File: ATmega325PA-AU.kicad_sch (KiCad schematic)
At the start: 19 parts, among them J1 1x3 straight header pins, J10 2Pin_Header_2.54, J2 1x3 straight header pins, J3 1x3 straight header pins, J4 1x3 straight header pins, J5 1x3 straight header pins, J6 1x3 straight header pins, J7 1x3 straight header pins, U2 ATMEGA325PA-AU, Y1 ABMM2-7.3728MHZ-E2-T

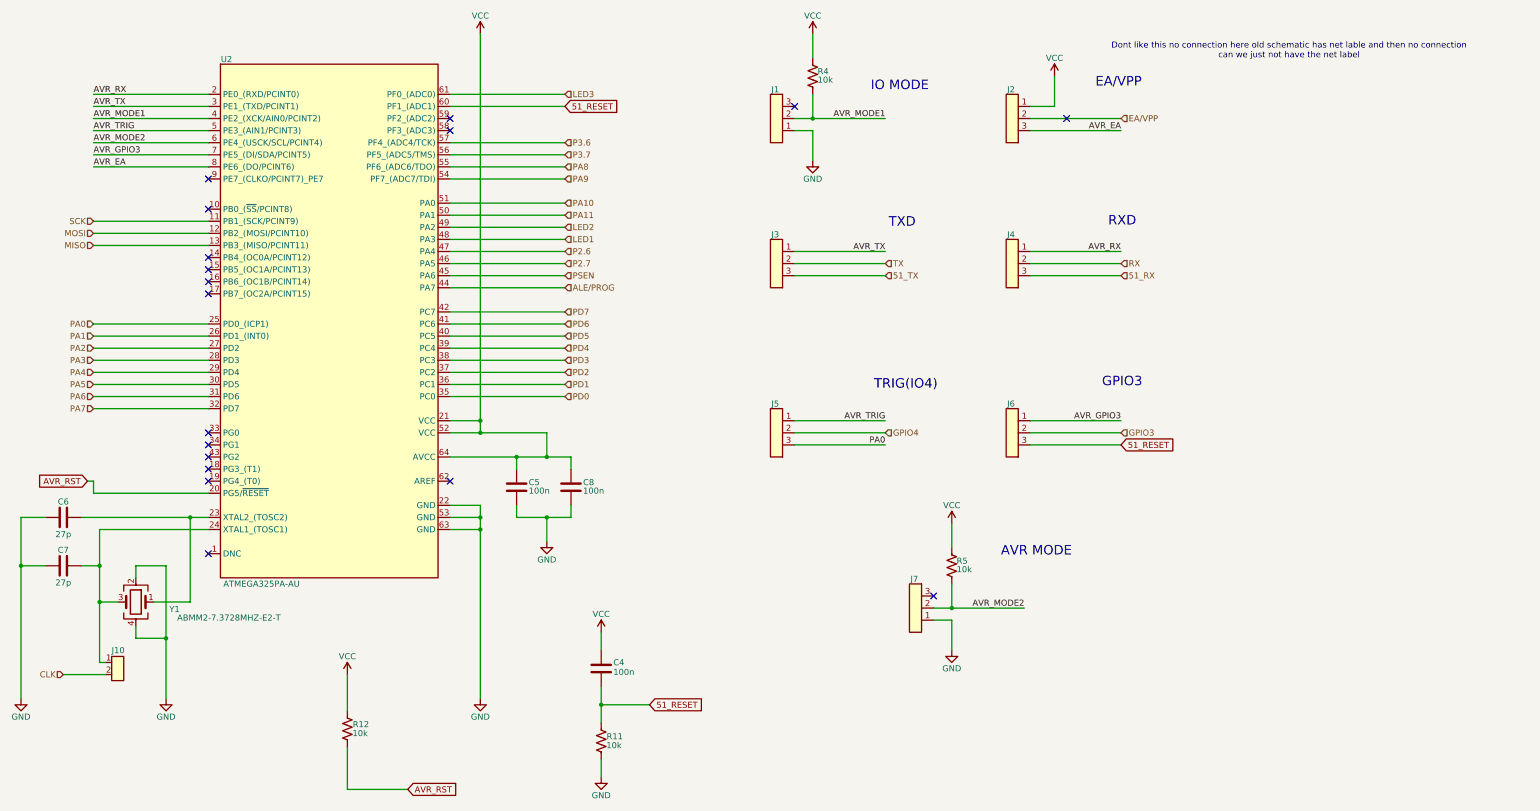
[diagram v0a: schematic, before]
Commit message: updated schematic after library re-organization
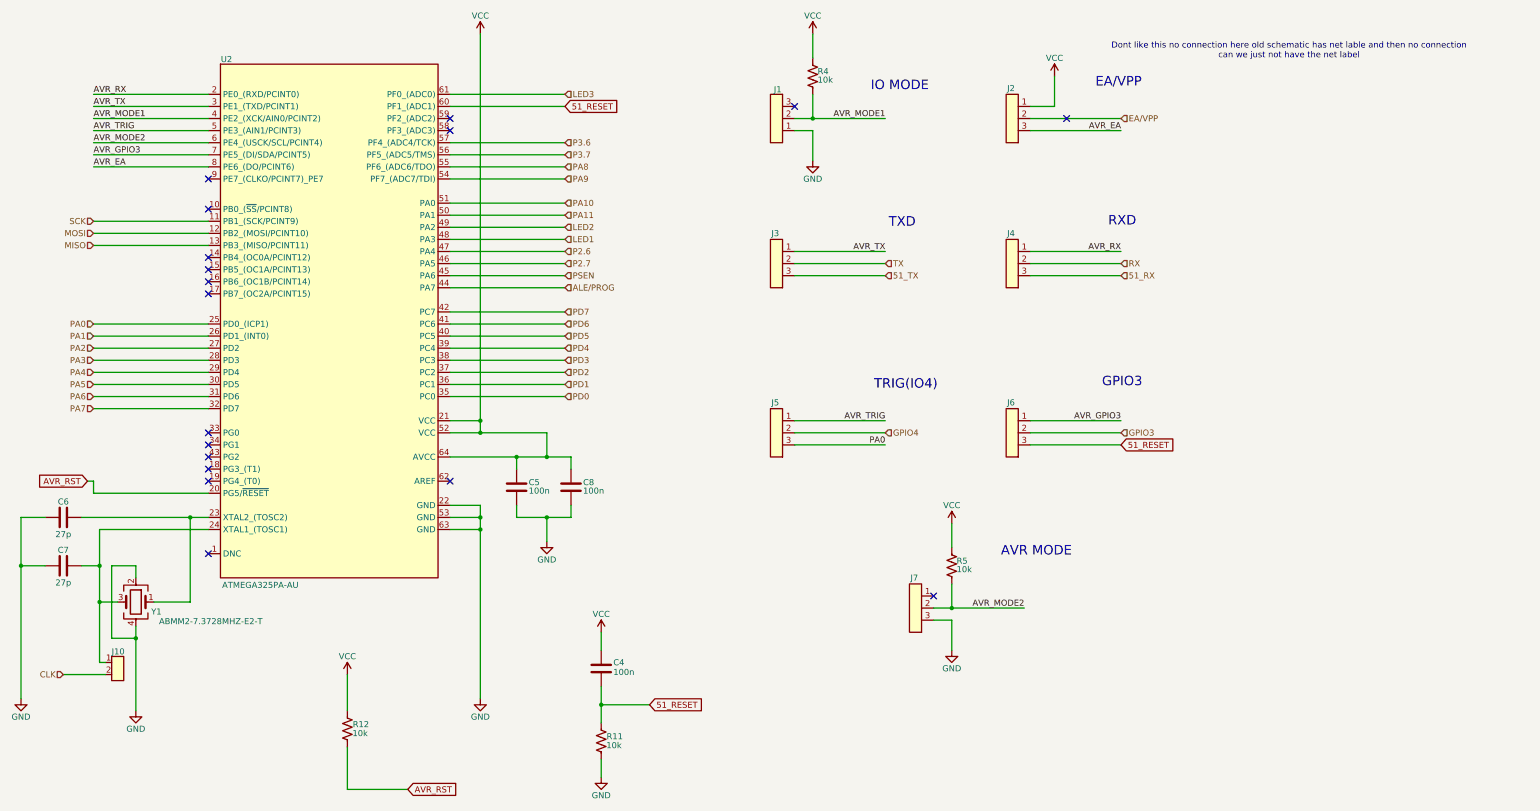
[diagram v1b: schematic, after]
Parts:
- removed J1, J2, J3, J4, J5, J6, J7: 1x3 straight header pins, Connector_PinHeader_2.54mm:PinHeader_1x03_P2.54mm_Vertical, symbol tutorial_2_library:VERT_HDR_3_2.54mm
- removed J10: 2Pin_Header_2.54, Connector_PinHeader_2.54mm:PinHeader_2x01_P2.54mm_Vertical, symbol tutorial_2_library:VERT_HDR_2_2.54mm
- removed U2: ATMEGA325PA-AU, Package_QFP:TQFP-64_10x10mm_P0.5mm, symbol tutorial_2_library:ATMEGA325PA-AU
- removed Y1: ABMM2-7.3728MHZ-E2-T, Crystal:Crystal_SMD_0603-4Pin_6.0x3.5mm, symbol tutorial_2_library:Crystal_7.3728MHZ_SMD
- added J1, J2, J3, J4, J5, J6, J7: 1x3 straight header pins, Connector_PinHeader_2.54mm:PinHeader_1x03_P2.54mm_Vertical, symbol NAE_Connectors:VERT_HDR_3_2.54mm
- added J10: 2Pin_Header_2.54, Connector_PinHeader_2.54mm:PinHeader_2x01_P2.54mm_Vertical, symbol NAE_Connectors:VERT_HDR_2_2.54mm
- added U2: ATMEGA325PA-AU, Package_QFP:TQFP-64_10x10mm_P0.5mm, symbol NAE_Integrated_Circuits:ATMEGA325PA-AU
- added Y1: ABMM2-7.3728MHZ-E2-T, Crystal:Crystal_SMD_0603-4Pin_6.0x3.5mm, symbol NAE_Crystals:Crystal_7.3728MHZ_SMD
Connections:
- net 51_RESET: now also J6.3, U2.60 (PF1_(ADC1))
- net 51_RX: now also J4.3
- net 51_TX: now also J3.3
- net ALE/PROG: now also U2.44 (PA7)
- net AVR_EA: now also J2.3, U2.8 (PE6_(DO/PCINT6))
- net AVR_GPIO3: now also J6.1, U2.7 (PE5_(DI/SDA/PCINT5))
- net AVR_MODE1: now also J1.2, U2.4 (PE2_(XCK/AIN0/PCINT2))
- net AVR_MODE2: now also J7.2, U2.6 (PE4_(USCK/SCL/PCINT4))
- net AVR_RST: now also U2.20 (PG5/~{RESET})
- net AVR_RX: now also J4.1, U2.2 (PE0_(RXD/PCINT0))
- net AVR_TRIG: now also J5.1, U2.5 (PE3_(AIN1/PCINT3))
- net AVR_TX: now also J3.1, U2.3 (PE1_(TXD/PCINT1))
- net CLK: now also J10.2
- net EA/VPP: now also J2.2
- net GND: now also J1.1, J7.3, U2.22 (GND), U2.53 (GND), U2.63 (GND), Y1.2, Y1.4
- net GPIO3: now also J6.2
- net GPIO4: now also J5.2
- net LED1: now also U2.48 (PA3)
- net LED2: now also U2.49 (PA2)
- net LED3: now also U2.61 (PF0_(ADC0))
- net MISO: now also U2.13 (PB3_(MISO/PCINT11))
- net MOSI: now also U2.12 (PB2_(MOSI/PCINT10))
- net P2.6: now also U2.47 (PA4)
- net P2.7: now also U2.46 (PA5)
- net P3.6: now also U2.57 (PF4_(ADC4/TCK))
- net P3.7: now also U2.56 (PF5_(ADC5/TMS))
- net PA0: now also J5.3, U2.25 (PD0_(ICP1))
- net PA1: now also U2.26 (PD1_(INT0))
- net PA10: now also U2.51 (PA0)
- net PA11: now also U2.50 (PA1)
- net PA2: now also U2.27 (PD2)
- net PA3: now also U2.28 (PD3)
- net PA4: now also U2.29 (PD4)
- net PA5: now also U2.30 (PD5)
- net PA6: now also U2.31 (PD6)
- net PA7: now also U2.32 (PD7)
- net PA8: now also U2.55 (PF6_(ADC6/TDO))
- net PA9: now also U2.54 (PF7_(ADC7/TDI))
- net PD0: now also U2.35 (PC0)
- net PD1: now also U2.36 (PC1)
- net PD2: now also U2.37 (PC2)
- net PD3: now also U2.38 (PC3)
- net PD4: now also U2.39 (PC4)
- net PD5: now also U2.40 (PC5)
- net PD6: now also U2.41 (PC6)
- net PD7: now also U2.42 (PC7)
- net PSEN: now also U2.45 (PA6)
- net RX: now also J4.2
- net SCK: now also U2.11 (PB1_(SCK/PCINT9))
- net TX: now also J3.2
- net VCC: now also J2.1, U2.21 (VCC), U2.52 (VCC), U2.64 (AVCC)
- net at C6.2: now also U2.23 (XTAL2_(TOSC2)), Y1.1
- net at C7.2: now also J10.1, U2.24 (XTAL1_(TOSC1)), Y1.3
